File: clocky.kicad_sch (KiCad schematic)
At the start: 76 parts, among them J1 Bot 50 pin, J2 Bot 40 pin, J3 Top 50 pin, J4 Top 40 pin, J5 Power, J6 JST_PH, J8 Program, Q1 AO3401A, U1 HEF4094B, U10 TMP117xxDRV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

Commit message: Do a round of tidy-up on clocky.
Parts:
- removed R5: 470, Resistor_SMD:R_0402_1005Metric, symbol Device:R
- added D5: 1N5819WS, Diode_SMD:D_SOD-323, symbol Diode:1N5819WS
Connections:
- net +BATT: now also D5.1 (K)
- net at F1.2, J6.1 (Pin_1): now also D5.2 (A)
- no-connect marks 22 -> 27
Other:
- moved on the sheet: F1
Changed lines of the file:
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@@
 	)
 	(junction
-		(at 39.37 78.74)
-		(diameter 0)
-		(color 0 0 0 0)
-	)
-	(junction
 		(at 64.77 101.6)
 		(diameter 0)
@@
 	)
 	(junction
-		(at 39.37 71.12)
-		(diameter 0)
-		(color 0 0 0 0)
-	)
-	(junction
 		(at 40.64 30.48)
 		(diameter 0)
@@
 	)
 	(junction
+		(at 43.18 78.74)
+		(diameter 0)
+		(color 0 0 0 0)
+	)
+	(junction
 		(at 222.25 111.76)
 		(diameter 0)
@@
 	)
 	(no_connect
+		(at 80.01 109.22)
+	)
+	(no_connect
+		(at 80.01 121.92)
+	)
+	(no_connect
+		(at 49.53 157.48)
+	)
+	(no_connect
 		(at 80.01 147.32)
 	)
@@
 	)
 	(no_connect
+		(at 80.01 137.16)
+	)
+	(no_connect
 		(at 177.8 77.47)
 	)
@@
 	)
 	(no_connect
+		(at 49.53 170.18)
+	)
+	(no_connect
 		(at 269.24 74.93)
 	)
@@
 	(wire
 		(pts
-			(xy 34.29 71.12) (xy 39.37 71.12)
+			(xy 36.83 71.12) (xy 43.18 71.12)
 		)
 		(stroke
@@
 	(wire
 		(pts
-			(xy 34.29 78.74) (xy 39.37 78.74)
+			(xy 36.83 78.74) (xy 43.18 78.74)
 		)
 		(stroke
@@
 	(wire
 		(pts
-			(xy 39.37 78.74) (xy 43.18 78.74)
-		)
-		(stroke
-			(width 0)
-			(type default)
-		)
-	)
-	(wire
-		(pts
 			(xy 158.75 137.16) (xy 158.75 142.24)
 		)
@@
 	(wire
 		(pts
-			(xy 39.37 71.12) (xy 43.18 71.12)
-		)
-		(stroke
-			(width 0)
-			(type default)
-		)
-	)
-	(wire
-		(pts
 			(xy 80.01 116.84) (xy 88.9 116.84)
 		)
@@
 	)
 	(symbol
+		(lib_id "Diode:1N5819WS")
+		(at 43.18 74.93 270)
+		(unit 1)
+		(exclude_from_sim no)
+		(in_bom yes)
+		(on_board yes)
+		(dnp no)
+		(property "Reference" "D5"
+			(at 41.91 77.47 90)
+			(effects
+				(font
+					(size 1.27 1.27)
+				)
+			)
+		)
+		(property "Value" "1N5819WS"
+			(at 46.482 77.47 0)
+			(effects
+				(font
+					(size 1.27 1.27)
+				)
+			)
+		)
+		(property "Footprint" "Diode_SMD:D_SOD-323"
+			(at 38.735 74.93 0)
+			(effects
+				(font
+					(size 1.27 1.27)
+				)
+				(hide yes)
+			)
+		)
+		(property "Datasheet" "https://datasheet.lcsc.com/lcsc/2204281430_Guangdong-Hottech-1N5819WS_C191023.pdf"
+			(at 43.18 74.93 0)
+			(effects
+				(font
+					(size 1.27 1.27)
+				)
+				(hide yes)
+			)
+		)
+		(property "Description" "40V 600mV@1A 1A SOD-323 Schottky Barrier Diodes, SOD-323"
+			(at 43.18 74.93 0)
+			(effects
+				(font
+					(size 1.27 1.27)
+				)
+				(hide yes)
+			)
+		)
+		(property "Sim.Device" "D"
+			(at 43.18 74.93 0)
+			(effects
+				(font
+					(size 1.27 1.27)
+				)
+				(hide yes)
+			)
+		)
+		(property "Sim.Pins" "1=K 2=A"
+			(at 43.18 74.93 0)
+			(effects
+				(font
+					(size 1.27 1.27)
+				)
+				(hide yes)
+			)
+		)
+		(property "JLCPCB" "C191023"
+			(at 43.18 74.93 0)
+			(effects
+				(font
+					(size 1.27 1.27)
+				)
+				(hide yes)
+			)
+		)
+		(pin "2"
+		)
+		(pin "1"
+		)
+		(instances
+			(project "clocky"
+				(path "/1a152c6d-723d-49c0-9a40-41d8f1ee1a82"
+					(reference "D5")
+					(unit 1)
+				)
+			)
+		)
+	)
+	(symbol
 		(lib_id "Device:C_Polarized")
 		(at 40.64 34.29 0)
@@
 	(symbol
 		(lib_id "Device:Polyfuse")
-		(at 34.29 74.93 0)
+		(at 36.83 74.93 0)
+		(mirror y)
 		(unit 1)
 		(exclude_from_sim no)
@@
 		(dnp no)
 		(property "Reference" "F1"
-			(at 31.75 74.93 90)
+			(at 39.37 74.93 90)
 			(effects
 				(font
@@
 		)
 		(property "Value" "116mA"
-			(at 36.83 74.93 90)
+			(at 34.29 74.93 90)
 			(effects
 				(font
@@
 		)
 		(property "Datasheet" "PRG21BB150MB1RK"
-			(at 34.29 74.93 0)
+			(at 36.83 74.93 0)
 			(effects
 				(font
@@
 		)
 		(property "Description" "Resettable fuse, polymeric positive temperature coefficient"
-			(at 34.29 74.93 0)
+			(at 36.83 74.93 0)
 			(effects
 				(font
@@
 		)
 		(property "JLCPCB" ""
-			(at 34.29 74.93 0)
+			(at 36.83 74.93 0)
 			(effects
 				(font
@@
 					(unit 1)
 				)
-			)
-		)
-	)
-	(symbol
-		(lib_id "Device:R")
-		(at 39.37 74.93 180)
-		(unit 1)
-		(exclude_from_sim no)
-		(in_bom yes)
-		(on_board yes)
-		(dnp no)
-		(property "Reference" "R5"
-			(at 39.37 70.104 0)
-			(effects
-				(font
-					(size 1.27 1.27)
-				)
-			)
-		)
-		(property "Value" "470"
-			(at 39.37 74.93 90)
-			(effects
-				(font
-					(size 1.27 1.27)
-				)
-			)
-		)
-		(property "Footprint" "Resistor_SMD:R_0402_1005Metric"
-			(at 41.148 74.93 90)
-			(effects
-				(font
-					(size 1.27 1.27)
-				)
-				(hide yes)
-			)
-		)
-		(property "Datasheet" "~"
-			(at 39.37 74.93 0)
-			(effects
-				(font
-					(size 1.27 1.27)
-				)
-				(hide yes)
-			)
-		)
-		(property "Description" "Resistor"
-			(at 39.37 74.93 0)
-			(effects
-				(font
-					(size 1.27 1.27)
-				)
-				(hide yes)
-			)
-		)
-		(property "JLCPCB" "C25117"
-			(at 39.37 74.93 0)
-			(effects
-				(font
-					(size 1.27 1.27)
-				)
-				(hide yes)
-			)
-		)
-		(pin "1"
-		)
-		(pin "2"
-		)
-		(instances
-			(project "clocky"
-				(path "/1a152c6d-723d-49c0-9a40-41d8f1ee1a82"
-					(reference "R5")
-					(unit 1)
-				)

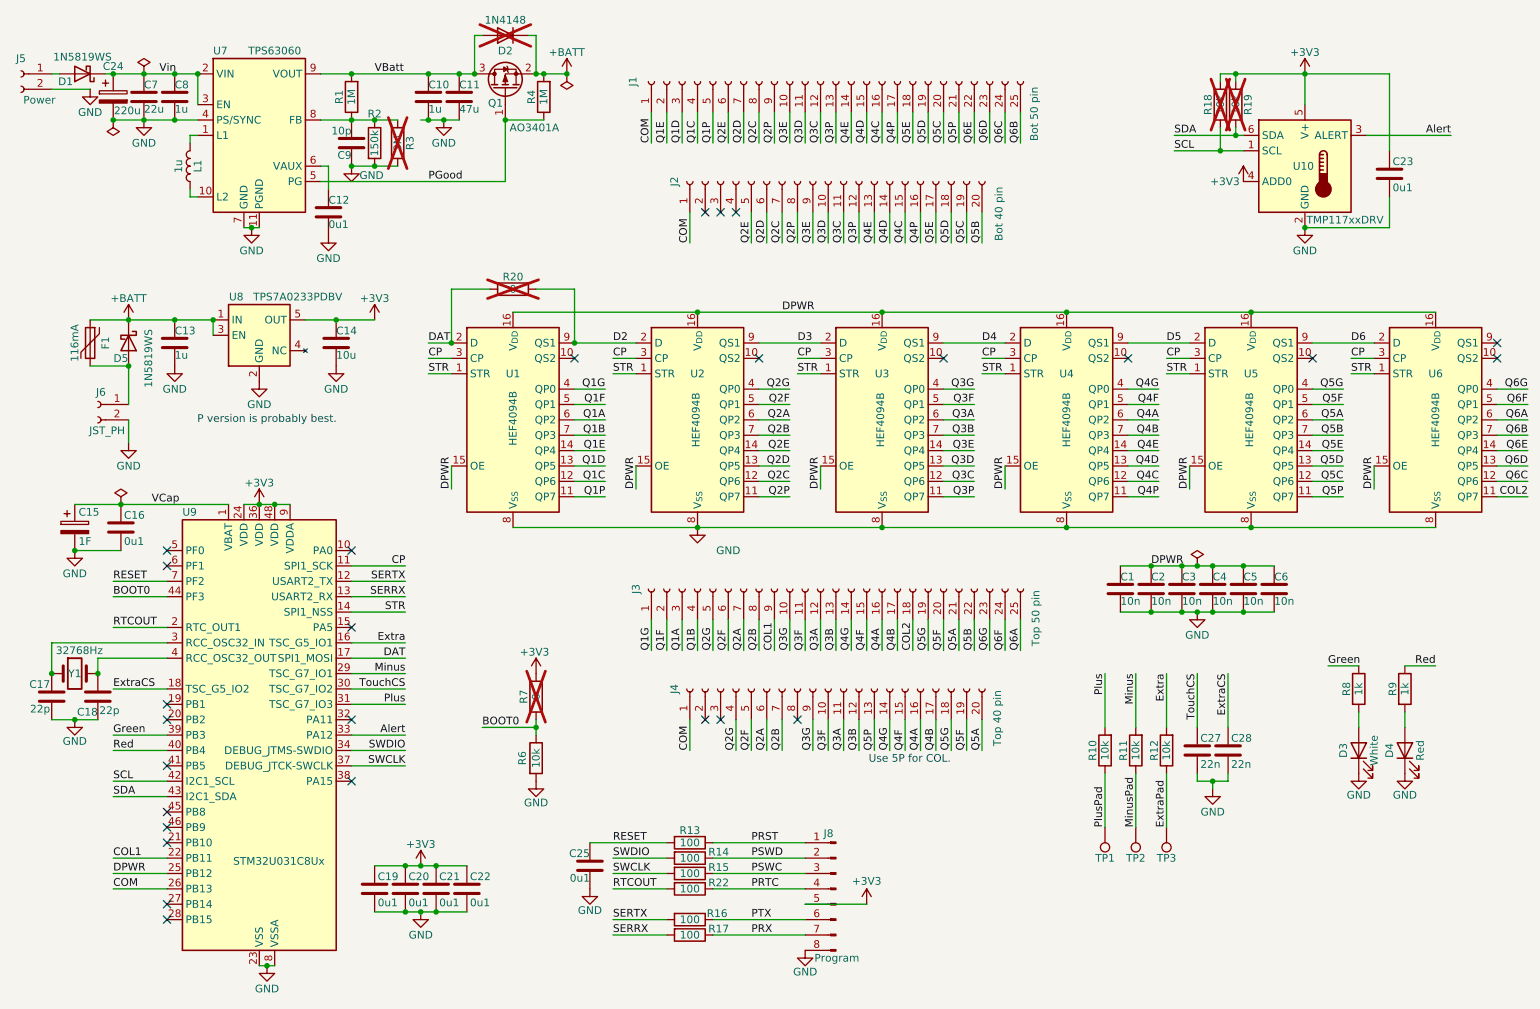
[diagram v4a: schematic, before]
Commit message: Rotate CPU on clocky.  Tidy up every where.
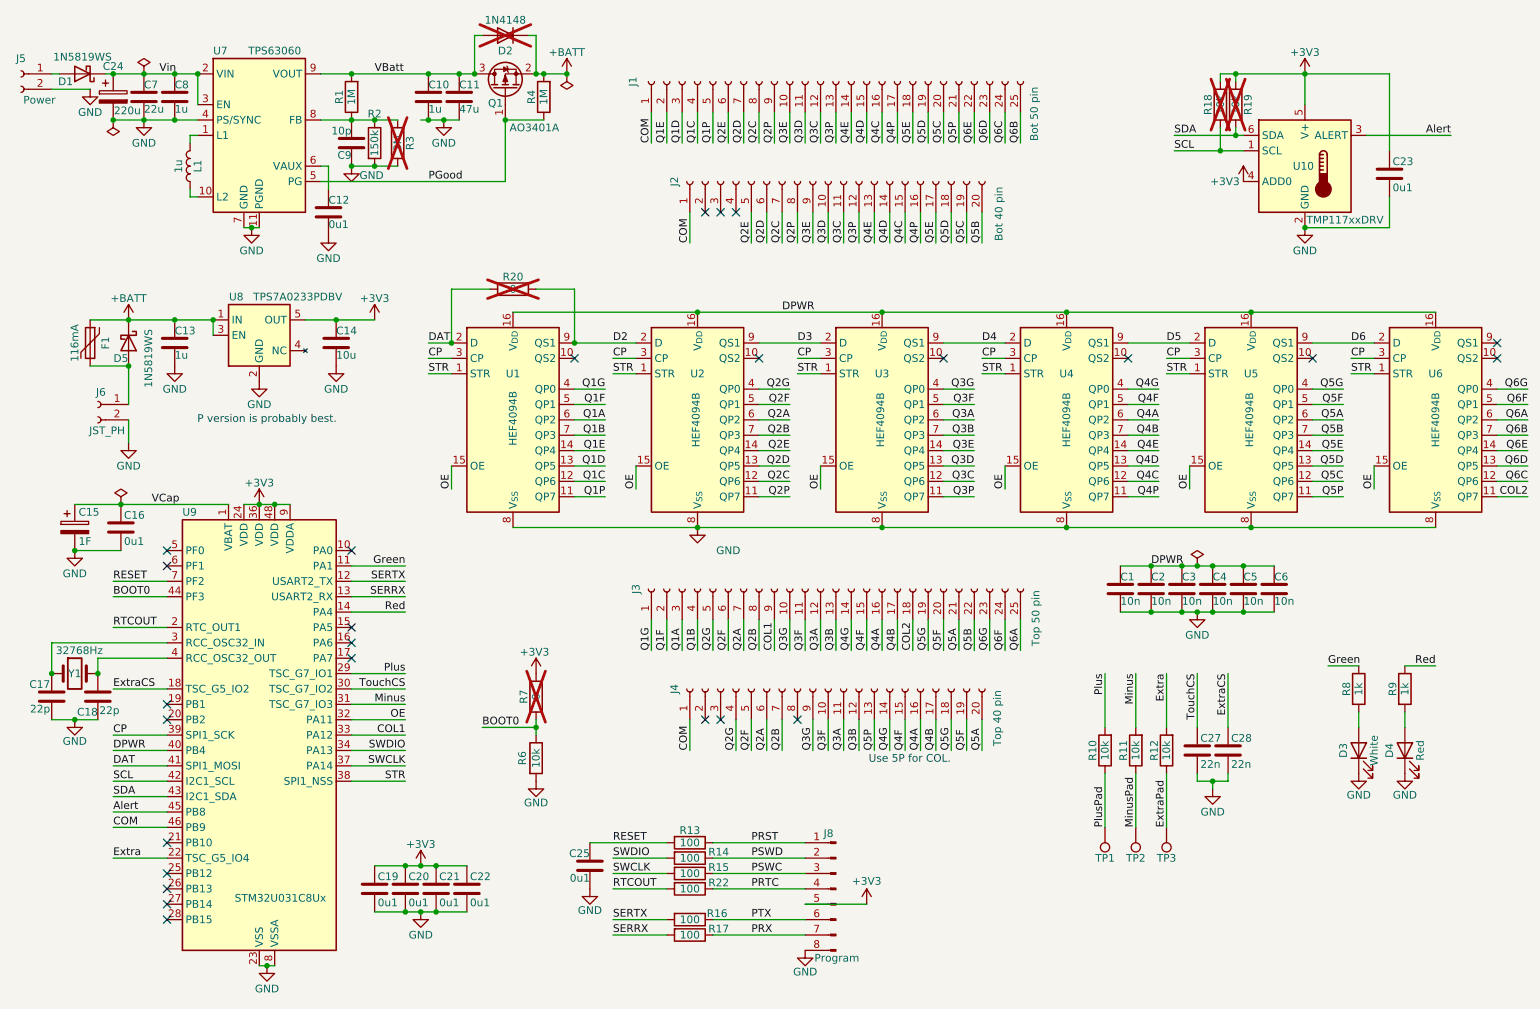
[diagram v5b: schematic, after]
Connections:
- net Alert: now also U9.45 (PB8); no longer U9.33 (PA12)
- net COL1: now also U9.33 (PA12); no longer U9.22 (PB11)
- net COM: now also U9.46 (PB9); no longer U9.26 (PB13)
- net CP: now also U9.39 (PB3); no longer U9.11 (PA1)
- net DAT: now also U9.41 (PB5); no longer U9.17 (PA7)
- net DPWR: now also U9.40 (PB4); no longer U1.15 (OE), U2.15 (OE), U3.15 (OE), U4.15 (OE), U5.15 (OE), U6.15 (OE), U9.25 (PB12)
- net Extra: now also U9.22 (PB11); no longer U9.16 (PA6)
- net Green: now also U9.11 (PA1); no longer U9.39 (PB3)
- net Minus: now also U9.31 (PA10); no longer U9.29 (PA8)
- net Plus: now also U9.29 (PA8); no longer U9.31 (PA10)
- net Red: now also U9.14 (PA4); no longer U9.40 (PB4)
- net STR: now also U9.38 (PA15); no longer U9.14 (PA4)
- net OE: now reaches U9.32 (PA11)
- net OE: now also U1.15 (OE), U2.15 (OE), U3.15 (OE), U4.15 (OE), U5.15 (OE), U6.15 (OE)
- no-connect marks 27 -> 26
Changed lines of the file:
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@@
 	)
 	(no_connect
-		(at 143.51 53.34)
+		(at 80.01 127)
 	)
 	(no_connect
-		(at 80.01 109.22)
+		(at 143.51 53.34)
 	)
 	(no_connect
-		(at 80.01 121.92)
+		(at 49.53 162.56)
 	)
 	(no_connect
-		(at 49.53 157.48)
+		(at 80.01 109.22)
 	)
 	(no_connect
-		(at 80.01 147.32)
+		(at 80.01 121.92)
 	)
 	(no_connect
@@
 	)
 	(no_connect
-		(at 80.01 137.16)
-	)
-	(no_connect
 		(at 177.8 77.47)
 	)
@@
 	)
 	(no_connect
+		(at 80.01 124.46)
+	)
+	(no_connect
 		(at 147.32 77.47)
 	)
@@
 	)
 	(no_connect
-		(at 49.53 144.78)
+		(at 238.76 77.47)
 	)
 	(no_connect
-		(at 49.53 154.94)
+		(at 49.53 165.1)
 	)
 	(no_connect
-		(at 238.76 77.47)
-	)
-	(no_connect
-		(at 49.53 152.4)
+		(at 49.53 157.48)
 	)
 	(no_connect
@@
 	(wire
 		(pts
-			(xy 88.9 127) (xy 80.01 127)
+			(xy 40.64 144.78) (xy 49.53 144.78)
 		)
 		(stroke
@@
 	(wire
 		(pts
-			(xy 40.64 139.7) (xy 49.53 139.7)
+			(xy 88.9 111.76) (xy 80.01 111.76)
 		)
 		(stroke
@@
 	(wire
 		(pts
+			(xy 80.01 137.16) (xy 88.9 137.16)
+		)
+		(stroke
+			(width 0)
+			(type default)
+		)
+	)
+	(wire
+		(pts
 			(xy 62.23 101.6) (xy 64.77 101.6)
 		)
@@
 	(wire
 		(pts
-			(xy 40.64 142.24) (xy 49.53 142.24)
+			(xy 88.9 119.38) (xy 80.01 119.38)
 		)
 		(stroke
@@
 	(wire
 		(pts
-			(xy 80.01 139.7) (xy 88.9 139.7)
+			(xy 49.53 152.4) (xy 40.64 152.4)
 		)
 		(stroke
@@
 	(wire
 		(pts
-			(xy 88.9 111.76) (xy 80.01 111.76)
+			(xy 40.64 139.7) (xy 49.53 139.7)
 		)
 		(stroke
@@
 	(wire
 		(pts
-			(xy 88.9 124.46) (xy 80.01 124.46)
+			(xy 40.64 160.02) (xy 49.53 160.02)
 		)
 		(stroke
@@
 	(wire
 		(pts
-			(xy 40.64 162.56) (xy 49.53 162.56)
+			(xy 40.64 142.24) (xy 49.53 142.24)
 		)
 		(stroke
@@
 	(wire
 		(pts
-			(xy 49.53 160.02) (xy 40.64 160.02)
+			(xy 80.01 139.7) (xy 88.9 139.7)
 		)
 		(stroke
@@
 	(wire
 		(pts
-			(xy 49.53 165.1) (xy 40.64 165.1)
+			(xy 49.53 154.94) (xy 40.64 154.94)
 		)
 		(stroke
@@
 	(wire
 		(pts
-			(xy 88.9 119.38) (xy 80.01 119.38)
+			(xy 88.9 147.32) (xy 80.01 147.32)
 		)
 		(stroke
@@
 	)
 	(label "STR"
-		(at 88.9 119.38 180)
+		(at 88.9 147.32 180)
 		(effects
 			(font
@@
 	)
 	(label "CP"
-		(at 88.9 111.76 180)
+		(at 40.64 139.7 0)
 		(effects
 			(font
 				(size 1.27 1.27)
 			)
-			(justify right bottom)
+			(justify left bottom)
 		)
 	)
@@
 	)
 	(label "Plus"
-		(at 88.9 134.62 180)
+		(at 88.9 129.54 180)
 		(effects
 			(font
@@
 		)
 	)
-	(label "DPWR"
+	(label "OE"
 		(at 248.92 99.06 90)
 		(effects
@@
 		)
 	)
-	(label "DPWR"
+	(label "OE"
 		(at 157.48 99.06 90)
 		(effects
@@
 	)
 	(label "Green"
-		(at 40.64 139.7 0)
+		(at 88.9 111.76 180)
 		(effects
 			(font
 				(size 1.27 1.27)
 			)
-			(justify left bottom)
+			(justify right bottom)
 		)
 	)
@@
 		)
 	)
-	(label "DPWR"
+	(label "OE"
 		(at 127 99.06 90)
 		(effects
@@
 	)
 	(label "Minus"
-		(at 88.9 129.54 180)
+		(at 88.9 134.62 180)
 		(effects
 			(font
@@
 	)
 	(label "COL1"
-		(at 40.64 160.02 0)
+		(at 88.9 139.7 180)
 		(effects
 			(font
 				(size 1.27 1.27)
 			)
-			(justify left bottom)
+			(justify right bottom)
 		)
 	)
@@
 		)
 	)
-	(label "DPWR"
+	(label "OE"
 		(at 218.44 99.06 90)
 		(effects
@@
 		)
 	)
-	(label "DPWR"
+	(label "OE"
+		(at 88.9 137.16 180)
+		(effects
+			(font
+				(size 1.27 1.27)
+			)
+			(justify right bottom)
+		)
+	)
+	(label "OE"
 		(at 96.52 99.06 90)
 		(effects
@@
 	)
 	(label "Red"
-		(at 40.64 142.24 0)
+		(at 88.9 119.38 180)
 		(effects
 			(font
 				(size 1.27 1.27)
 			)
-			(justify left bottom)
+			(justify right bottom)
 		)
 	)
@@
 	)
 	(label "DAT"
-		(at 88.9 127 180)
+		(at 40.64 144.78 0)
 		(effects
 			(font
 				(size 1.27 1.27)
 			)
-			(justify right bottom)
+			(justify left bottom)
 		)
 	)
@@
 	)
 	(label "Extra"
-		(at 88.9 124.46 180)
+		(at 40.64 160.02 0)
 		(effects
 			(font
 				(size 1.27 1.27)
 			)
-			(justify right bottom)
+			(justify left bottom)
 		)
 	)
@@
 	)
 	(label "Alert"
-		(at 88.9 139.7 180)
+		(at 40.64 152.4 0)
 		(effects
 			(font
 				(size 1.27 1.27)
 			)
-			(justify right bottom)
+			(justify left bottom)
 		)
 	)
@@
 	)
 	(label "DPWR"
-		(at 40.64 162.56 0)
+		(at 40.64 142.24 0)
 		(effects
 			(font
@@
 		)
 	)
-	(label "DPWR"
+	(label "OE"
 		(at 187.96 99.06 90)
 		(effects
@@
 	)
 	(label "COM"
-		(at 40.64 165.1 0)
+		(at 40.64 154.94 0)
 		(effects
 			(font
@@
 		)
 		(property "Value" "STM32U031C8Ux"
-			(at 60.452 160.528 0)
+			(at 60.706 166.624 0)
 			(effects
 				(font
@@
 		)
 		(pin "38"
+			(alternate "SPI1_NSS")
 		)
 		(pin "18"
@@
 		)
 		(pin "41"
+			(alternate "SPI1_MOSI")
 		)
 		(pin "48"
 		)
 		(pin "34"
-			(alternate "DEBUG_JTMS-SWDIO")
 		)
 		(pin "11"
-			(alternate "SPI1_SCK")
 		)
 		(pin "45"
@@
 		)
 		(pin "17"
-			(alternate "SPI1_MOSI")
 		)
 		(pin "26"
@@
 		)
 		(pin "22"
+			(alternate "TSC_G5_IO4")
 		)
 		(pin "23"
@@
 		)
 		(pin "39"
+			(alternate "SPI1_SCK")
 		)
 		(pin "40"
 		)
 		(pin "14"
-			(alternate "SPI1_NSS")
 		)
 		(pin "16"
-			(alternate "TSC_G5_IO1")
 		)
 		(pin "42"
@@
 		)
 		(pin "37"
-			(alternate "DEBUG_JTCK-SWCLK")
 		)
 		(pin "15"

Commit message: Tweak power & zones.
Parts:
- added D6: 1N4148, Diode_SMD:D_0603_1608Metric, symbol Device:D
- added R5: 100, Resistor_SMD:R_0603_1608Metric, symbol Device:R
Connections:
- net +3V3: now also D6.2 (A)
- net VCap: now also D6.1 (K), R5.2; no longer C15.1
- new net: C15.1, R5.1
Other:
- moved on the sheet: D5, F1, J6
